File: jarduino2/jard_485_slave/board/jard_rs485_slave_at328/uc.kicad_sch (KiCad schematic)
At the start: 13 parts, among them J7 ISCP, U5 ATmega328P-A, Y1 Resonator

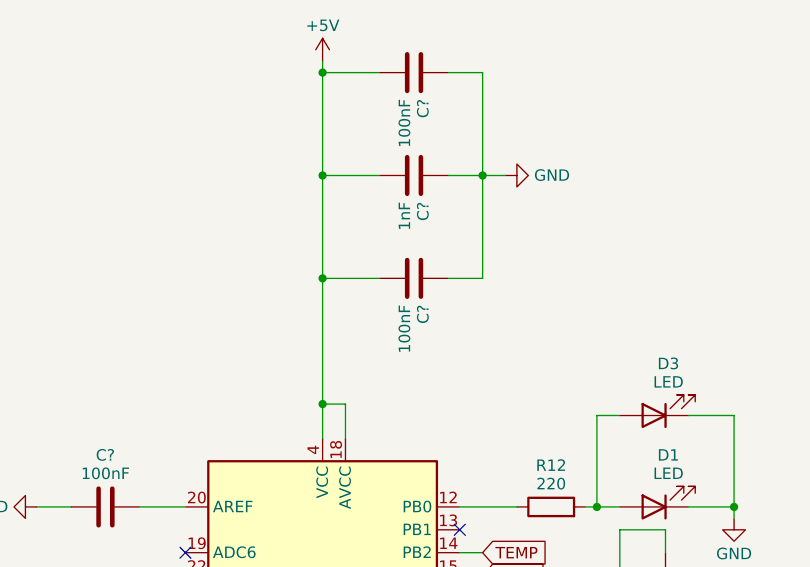
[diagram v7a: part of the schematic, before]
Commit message: Changement empreinte de D2 (trous + gros et 12mm long) Dessin sérigraphie J2 (sens de la sonde)
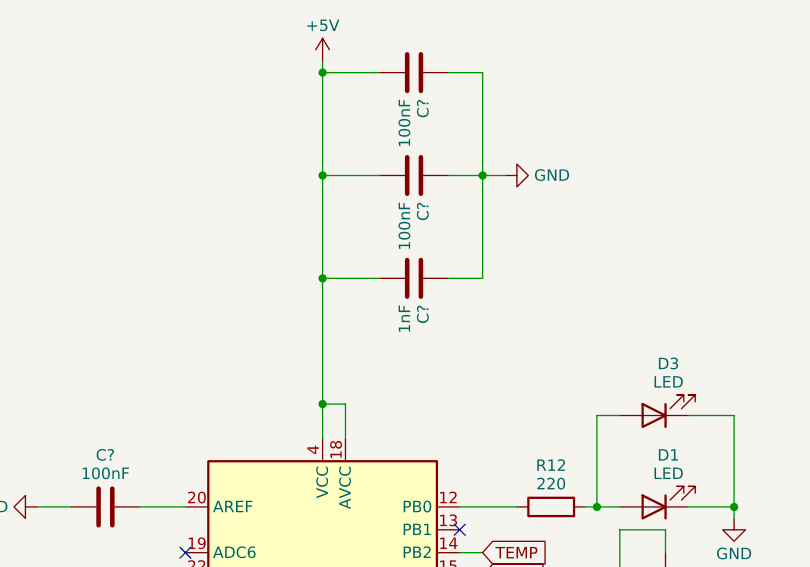
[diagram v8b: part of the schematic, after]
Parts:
- C? (x2): RefFabricant C0603X102J5GACAUTO -> C0603C104K1RACTU; RefFournisseur 2219417 -> 4199453
- C?: value 100nF -> 1nF
- C?: value 1nF -> 100nF; RefFabricant C0603X102J5GACAUTO -> C0603C104K1RACTU; RefFournisseur 2219417 -> 4199453
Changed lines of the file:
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@@
       (effects (font (size 1.27 1.27)) hide)
     )
-    (property "RefFabricant" "C0603X102J5GACAUTO" (at 109.22 95.25 0)
-      (effects (font (size 1.27 1.27)) hide)
-    )
-    (property "RefFournisseur" "2219417" (at 109.22 95.25 0)
+    (property "RefFabricant" "C0603C104K1RACTU" (at 109.22 95.25 0)
+      (effects (font (size 1.27 1.27)) hide)
+    )
+    (property "RefFournisseur" "4199453" (at 109.22 95.25 0)
       (effects (font (size 1.27 1.27)) hide)
     )
@@
       (effects (font (size 1.27 1.27)) (justify left))
     )
-    (property "Value" "100nF" (at 142.486 72.771 0)
+    (property "Value" "1nF" (at 142.486 72.771 0)
       (effects (font (size 1.27 1.27)) (justify left))
     )
@@
       (effects (font (size 1.27 1.27)) hide)
     )
-    (property "Description" "Condensateur céramique 100nF" (at 143.51 69.85 0)
+    (property "Description" "Condensateur céramique 1nF" (at 143.51 69.85 0)
       (effects (font (size 1.27 1.27)) hide)
     )
@@
       (effects (font (size 1.27 1.27)) (justify left))
     )
-    (property "Value" "1nF" (at 142.486 61.341 0)
+    (property "Value" "100nF" (at 142.486 61.341 0)
       (effects (font (size 1.27 1.27)) (justify left))
     )
@@
       (effects (font (size 1.27 1.27)) hide)
     )
-    (property "RefFabricant" "C0603X102J5GACAUTO" (at 143.51 58.42 0)
-      (effects (font (size 1.27 1.27)) hide)
-    )
-    (property "RefFournisseur" "2219417" (at 143.51 58.42 0)
+    (property "RefFabricant" "C0603C104K1RACTU" (at 143.51 58.42 0)
+      (effects (font (size 1.27 1.27)) hide)
+    )
+    (property "RefFournisseur" "4199453" (at 143.51 58.42 0)
       (effects (font (size 1.27 1.27)) hide)
     )
@@
       (effects (font (size 1.27 1.27)) hide)
     )
-    (property "Description" "Condensateur céramique 1nF" (at 143.51 58.42 0)
+    (property "Description" "Condensateur céramique 100nF" (at 143.51 58.42 0)
       (effects (font (size 1.27 1.27)) hide)
     )
@@
       (effects (font (size 1.27 1.27)) hide)
     )
-    (property "RefFabricant" "C0603X102J5GACAUTO" (at 143.51 46.99 0)
-      (effects (font (size 1.27 1.27)) hide)
-    )
-    (property "RefFournisseur" "2219417" (at 143.51 46.99 0)
-      (effects (font (size 1.27 1.27)) hide)
-    )
+    (property "RefFabricant" "C0603C104K1RACTU" (at 143.51 46.99 0)
+      (effects (font (size 1.27 1.27)) hide)
+    )
+    (property "RefFournisseur" "4199453" (at 143.51 46.99 0)
+      (effects (font (size 1.27 1.27)) hide)
+    )
